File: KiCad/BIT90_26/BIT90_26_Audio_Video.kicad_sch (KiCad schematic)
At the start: 14 parts, among them Q1 2N2222, U1 SN76489AN, U16 Pico9918

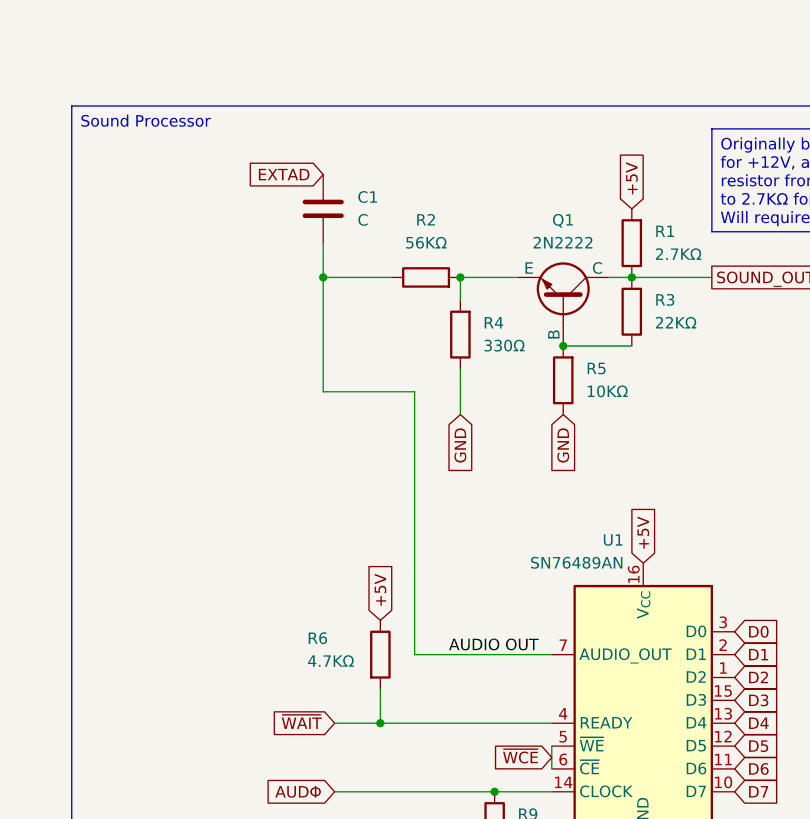
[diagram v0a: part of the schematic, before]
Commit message: Minor corrections & footprints assigned
PCB layout started
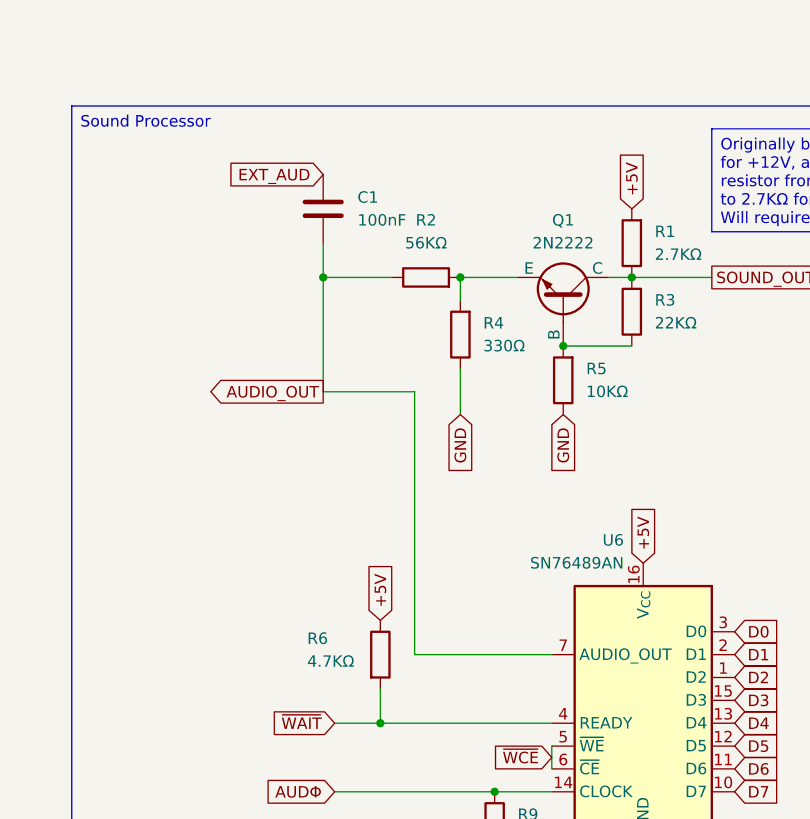
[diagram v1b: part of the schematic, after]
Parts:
- C1: value C -> 100nF; footprint (none) -> Capacitor_THT:C_Disc_D3.4mm_W2.1mm_P2.50mm
- C4: footprint (none) -> Capacitor_THT:C_Disc_D3.4mm_W2.1mm_P2.50mm
- D1: footprint (none) -> Diode_THT:D_DO-35_SOD27_P7.62mm_Horizontal
- Q1: footprint (none) -> Package_TO_SOT_THT:TO-92_Inline_Wide
- R1, R10, R2, R3, R4, R5, R6, R9: footprint (none) -> Resistor_THT:R_Axial_DIN0207_L6.3mm_D2.5mm_P7.62mm_Horizontal
- renumbered U1 to U6
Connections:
- net AUDIO OUT renamed AUDIO_OUT
- net EXTAD renamed EXT_AUD
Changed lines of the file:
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@@
 	(title_block
 		(title "BIT90/26 Computer - Audio & Video")
-		(date "5/JUN/2026")
+		(date "6/JUN/2026")
 		(rev "WIP")
 		(company "Brett Hallen")
@@
 		)
 	)
-	(label "AUDIO OUT"
-		(at 264.16 140.97 0)
-		(effects
-			(font
-				(size 1.27 1.27)
-			)
-			(justify left bottom)
-		)
-	)
 	(global_label "D3"
 		(shape input)
@@
 		)
 	)
-	(global_label "EXTAD"
+	(global_label "EXT_AUD"
 		(shape input)
 		(at 250.19 87.63 180)
@@
 				)
 				(justify left)
+				(hide yes)
+			)
+		)
+	)
+	(global_label "AUDIO_OUT"
+		(shape output)
+		(at 250.19 111.76 180)
+		(fields_autoplaced yes)
+		(effects
+			(font
+				(size 1.27 1.27)
+			)
+			(justify right)
+		)
+		(property "Intersheetrefs" "${INTERSHEET_REFS}"
+			(at 236.9842 111.76 0)
+			(effects
+				(font
+					(size 1.27 1.27)
+				)
+				(justify right)
 				(hide yes)
 			)
@@
 			)
 		)
-		(property "Footprint" ""
+		(property "Footprint" "Diode_THT:D_DO-35_SOD27_P7.62mm_Horizontal"
 			(at 115.57 106.68 0)
 			(effects
@@
 			)
 		)
-		(property "Footprint" ""
+		(property "Footprint" "Resistor_THT:R_Axial_DIN0207_L6.3mm_D2.5mm_P7.62mm_Horizontal"
 			(at 286.258 95.25 90)
 			(effects
@@
 			)
 		)
-		(property "Footprint" ""
+		(property "Footprint" "Resistor_THT:R_Axial_DIN0207_L6.3mm_D2.5mm_P7.62mm_Horizontal"
 			(at 261.62 100.838 90)
 			(effects
@@
 			)
 		)
-		(property "Footprint" ""
+		(property "Footprint" "Resistor_THT:R_Axial_DIN0207_L6.3mm_D2.5mm_P7.62mm_Horizontal"
 			(at 254.762 140.97 90)
 			(effects
@@
 			)
 		)
-		(property "Footprint" ""
+		(property "Footprint" "Capacitor_THT:C_Disc_D3.4mm_W2.1mm_P2.50mm"
 			(at 106.3752 118.11 0)
 			(effects
@@
 		(on_board yes)
 		(dnp no)
-		(property "Reference" "U1"
+		(property "Reference" "U6"
 			(at 283.6067 128.27 0)
 			(effects
@@
 			(project "BIT90_26"
 				(path "/d65498c3-6385-4920-ac0f-4c76daf90780/a2197f6c-13b4-44bf-8904-5835f7bd7927"
-					(reference "U1")
+					(reference "U6")
 					(unit 1)
 				)
@@
 			)
 		)
-		(property "Footprint" ""
+		(property "Footprint" "Resistor_THT:R_Axial_DIN0207_L6.3mm_D2.5mm_P7.62mm_Horizontal"
 			(at 286.258 102.87 90)
 			(effects
@@
 			)
 		)
-		(property "Footprint" ""
+		(property "Footprint" "Resistor_THT:R_Axial_DIN0207_L6.3mm_D2.5mm_P7.62mm_Horizontal"
 			(at 267.462 160.02 90)
 			(effects
@@
 			)
 		)
-		(property "Footprint" ""
+		(property "Footprint" "Resistor_THT:R_Axial_DIN0207_L6.3mm_D2.5mm_P7.62mm_Horizontal"
 			(at 278.638 110.49 90)
 			(effects
@@
 			)
 		)
-		(property "Footprint" ""
+		(property "Footprint" "Package_TO_SOT_THT:TO-92_Inline_Wide"
 			(at 276.86 38.1 0)
 			(effects
@@
 			)
 		)
-		(property "Footprint" ""
+		(property "Footprint" "Resistor_THT:R_Axial_DIN0207_L6.3mm_D2.5mm_P7.62mm_Horizontal"
 			(at 267.208 105.41 90)
 			(effects
@@
 			)
 		)
-		(property "Footprint" ""
+		(property "Footprint" "Resistor_THT:R_Axial_DIN0207_L6.3mm_D2.5mm_P7.62mm_Horizontal"
 			(at 103.632 106.68 90)
 			(effects
@@
 			)
 		)
-		(property "Value" "C"
+		(property "Value" "100nF"
 			(at 254 92.7099 0)
 			(effects
@@
 			)
 		)
-		(property "Footprint" ""
+		(property "Footprint" "Capacitor_THT:C_Disc_D3.4mm_W2.1mm_P2.50mm"
 			(at 251.1552 95.25 0)
 			(effects
